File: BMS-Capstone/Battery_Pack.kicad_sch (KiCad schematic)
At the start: 0 parts

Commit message: Added cells
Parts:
- added BT1, BT2, BT3, BT4, BT5, BT6, BT7: Battery_Cell, cell:keystone 254 18650, symbol Device:Battery_Cell
- added J1: Conn_01x12_Socket, symbol Connector:Conn_01x12_Socket
- added J2: Conn_01x02_Socket, symbol Connector:Conn_01x02_Socket
- added K1: J107F1CS203VDC.80, Relay_THT:Relay_SPST-NO_Fujitsu_FTR-LYAA005x_FormA_Vertical, symbol Relay:Fujitsu_FTR-LYAA005x
- added TH1, TH2, TH3: Thermistor, symbol Device:Thermistor
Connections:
- new net: BT1.1 (+), BT2.2 (-), J1.2 (Pin_2)
- new net: BT4.1 (+), BT5.2 (-), J1.5 (Pin_5)
- new net: BT3.1 (+), BT4.2 (-), J1.4 (Pin_4)
- new net: BT6.1 (+), BT7.2 (-), J1.7 (Pin_7)
- new net: BT5.1 (+), BT6.2 (-), J1.6 (Pin_6)
- new net: BT2.1 (+), BT3.2 (-), J1.3 (Pin_3)
- new net: BT7.1 (+), J1.8 (Pin_8), K1.13
- new net: J1.9 (Pin_9), K1.A1
- new net: J2.1 (Pin_1), K1.14
- new net GND: BT1.2 (-), J1.1 (Pin_1), J2.2 (Pin_2), K1.A2, TH1.2, TH2.2, TH3.2
- new net TH1: J1.10 (Pin_10), TH1.1
- new net TH2: J1.11 (Pin_11), TH2.1
- new net TH3: J1.12 (Pin_12), TH3.1

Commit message: Routed Cell Board
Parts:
- removed K1: J107F1CS203VDC.80, Relay_THT:Relay_SPST-NO_Fujitsu_FTR-LYAA005x_FormA_Vertical, symbol Relay:Fujitsu_FTR-LYAA005x
- added K1: J107F1CS203VDC.80, cell:3_3v relay, symbol Relay:DIPxx-1Cxx-51x
- J1: footprint (none) -> Connector_PinHeader_2.54mm:PinHeader_1x12_P2.54mm_Vertical
- J2: footprint (none) -> cell:XT60
- TH1, TH2, TH3: footprint (none) -> Resistor_THT:R_Axial_DIN0204_L3.6mm_D1.6mm_P2.54mm_Vertical
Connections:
- net GND: now also K1.2
- net at BT7.1 (+), J1.8 (Pin_8): now also K1.7, K1.8
- net at J1.9 (Pin_9): now also K1.6
- net at J2.1 (Pin_1): now also K1.14
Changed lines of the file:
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@@
+	)
+	(symbol
+		(lib_id "Relay:DIPxx-1Cxx-51x")
+		(at 129.54 57.15 0)
+		(unit 1)
+		(exclude_from_sim no)
+		(in_bom yes)
+		(on_board yes)
+		(dnp no)
+		(fields_autoplaced yes)
+		(property "Reference" "K1"
+			(at 140.97 55.8799 0)
+			(effects
+				(font
+					(size 1.27 1.27)
+				)
+				(justify left)
+			)
+		)
+		(property "Value" "J107F1CS203VDC.80"
+			(at 140.97 58.4199 0)
+			(effects
+				(font
+					(size 1.27 1.27)
+				)
+				(justify left)
+			)
+		)
+		(property "Footprint" "cell:3_3v relay"
+			(at 140.97 58.42 0)
+			(effects
+				(font
+					(size 1.27 1.27)
+				)
+				(justify left)
+				(hide yes)
+			)
+		)
+		(property "Datasheet" "https://standexelectronics.com/wp-content/uploads/datasheet_reed_relay_DIP.pdf"
+			(at 129.54 57.15 0)
+			(effects
+				(font
+					(size 1.27 1.27)
+				)
+				(hide yes)
+			)
+		)
+		(property "Description" "Standex Meder DIP reed relay, SPDT"
+			(at 129.54 57.15 0)
+			(effects
+				(font
+					(size 1.27 1.27)
+				)
+				(hide yes)
+			)
+		)
+		(pin "1"
+		)
+		(pin "8"
+		)
+		(pin "6"
+		)
+		(pin "14"
+		)
+		(pin "7"
+		)
+		(pin "2"
+		)
+		(instances
+			(project ""
+				(path "/f2da9442-ca05-4687-a880-d5cd24c39f1d/cf34981b-cbae-442d-9f72-9ae4895e9d63"
+					(reference "K1")
+					(unit 1)
+				)
+			)
+		)
 	)
 	(symbol
@@
 			)
 		)
-		(property "Footprint" ""
+		(property "Footprint" "Connector_PinHeader_2.54mm:PinHeader_1x12_P2.54mm_Vertical"
 			(at 50.8 111.76 0)
 			(effects
@@
 	)
 	(symbol
-		(lib_id "Relay:Fujitsu_FTR-LYAA005x")
-		(at 129.54 57.15 0)
-		(unit 1)
-		(exclude_from_sim no)
-		(in_bom yes)
-		(on_board yes)
-		(dnp no)
-		(fields_autoplaced yes)
-		(property "Reference" "K1"
-			(at 140.97 55.8799 0)
-			(effects
-				(font
-					(size 1.27 1.27)
-				)
-				(justify left)
-			)
-		)
-		(property "Value" "J107F1CS203VDC.80"
-			(at 140.97 58.4199 0)
-			(effects
-				(font
-					(size 1.27 1.27)
-				)
-				(justify left)
-			)
-		)
-		(property "Footprint" "Relay_THT:Relay_SPST-NO_Fujitsu_FTR-LYAA005x_FormA_Vertical"
-			(at 140.97 58.42 0)
-			(effects
-				(font
-					(size 1.27 1.27)
-				)
-				(justify left)
-				(hide yes)
-			)
-		)
-		(property "Datasheet" "https://www.fujitsu.com/sg/imagesgig5/ftr-ly.pdf"
-			(at 147.32 60.96 0)
-			(effects
-				(font
-					(size 1.27 1.27)
-				)
-				(justify left)
-				(hide yes)
-			)
-		)
-		(property "Description" "Relay, SPST Form A, vertical mount, 5-60V coil, 6A, 250VAC, 28 x 5 x 15mm"
-			(at 129.54 57.15 0)
-			(effects
-				(font
-					(size 1.27 1.27)
-				)
-				(hide yes)
-			)
-		)
-		(pin "A1"
-		)
-		(pin "A2"
-		)
-		(pin "13"
-		)
-		(pin "14"
-		)
-		(instances
-			(project ""
-				(path "/f2da9442-ca05-4687-a880-d5cd24c39f1d/cf34981b-cbae-442d-9f72-9ae4895e9d63"
-					(reference "K1")
-					(unit 1)
-				)
-			)
-		)
-	)
-	(symbol
 		(lib_id "Device:Battery_Cell")
 		(at 134.62 104.14 0)
@@
 			)
 		)
-		(property "Footprint" ""
+		(property "Footprint" "Resistor_THT:R_Axial_DIN0204_L3.6mm_D1.6mm_P2.54mm_Vertical"
 			(at 157.48 80.01 0)
 			(effects
@@
 			)
 		)
-		(property "Footprint" ""
+		(property "Footprint" "Resistor_THT:R_Axial_DIN0204_L3.6mm_D1.6mm_P2.54mm_Vertical"
 			(at 157.48 114.3 0)
 			(effects
@@
 			)
 		)
-		(property "Footprint" ""
+		(property "Footprint" "Resistor_THT:R_Axial_DIN0204_L3.6mm_D1.6mm_P2.54mm_Vertical"
 			(at 157.48 151.13 0)
 			(effects
@@
 			)
 		)
-		(property "Footprint" ""
+		(property "Footprint" "cell:XT60"
 			(at 137.16 38.1 0)
 			(effects

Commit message: Added fuse
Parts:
- added F1: Fuse, Fuse:Fuseholder_Blade_Mini_Keystone_3568, symbol Device:Fuse
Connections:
- net GND: now also F1.2; no longer BT1.2 (-), J1.1 (Pin_1)
- new net: BT1.2 (-), F1.1, J1.1 (Pin_1)
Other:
- moved on the sheet: J2, K1
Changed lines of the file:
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@@
+	)
+	(junction
+		(at 134.62 72.39)
+		(diameter 0)
+		(color 0 0 0 0)
 	)
 	(junction
@@
 	)
 	(junction
-		(at 134.62 72.39)
-		(diameter 0)
-		(color 0 0 0 0)
-	)
-	(junction
 		(at 134.62 121.92)
 		(diameter 0)
@@
 	(wire
 		(pts
+			(xy 134.62 167.64) (xy 134.62 166.37)
+		)
+		(stroke
+			(width 0)
+			(type default)
+		)
+	)
+	(wire
+		(pts
 			(xy 134.62 121.92) (xy 100.33 121.92)
 		)
@@
 	(wire
 		(pts
+			(xy 134.62 59.69) (xy 134.62 72.39)
+		)
+		(stroke
+			(width 0)
+			(type default)
+		)
+	)
+	(wire
+		(pts
 			(xy 134.62 148.59) (xy 134.62 147.32)
 		)
@@
 	(wire
 		(pts
-			(xy 134.62 64.77) (xy 134.62 72.39)
-		)
-		(stroke
-			(width 0)
-			(type default)
-		)
-	)
-	(wire
-		(pts
 			(xy 88.9 72.39) (xy 134.62 72.39)
 		)
@@
 	(wire
 		(pts
-			(xy 85.09 104.14) (xy 85.09 49.53)
+			(xy 85.09 104.14) (xy 85.09 44.45)
 		)
 		(stroke
@@
 	(wire
 		(pts
-			(xy 85.09 49.53) (xy 124.46 49.53)
+			(xy 85.09 44.45) (xy 124.46 44.45)
+		)
+		(stroke
+			(width 0)
+			(type default)
+		)
+	)
+	(wire
+		(pts
+			(xy 134.62 158.75) (xy 134.62 156.21)
 		)
 		(stroke
@@
 	(wire
 		(pts
-			(xy 137.16 43.18) (xy 137.16 49.53)
+			(xy 137.16 38.1) (xy 137.16 44.45)
 		)
 		(stroke
@@
 	(symbol
 		(lib_id "Relay:DIPxx-1Cxx-51x")
-		(at 129.54 57.15 0)
+		(at 129.54 52.07 0)
 		(unit 1)
 		(exclude_from_sim no)
@@
 		(fields_autoplaced yes)
 		(property "Reference" "K1"
-			(at 140.97 55.8799 0)
+			(at 140.97 50.7999 0)
 			(effects
 				(font
@@
 		)
 		(property "Value" "J107F1CS203VDC.80"
-			(at 140.97 58.4199 0)
+			(at 140.97 53.3399 0)
 			(effects
 				(font
@@
 		)
 		(property "Footprint" "cell:3_3v relay"
-			(at 140.97 58.42 0)
+			(at 140.97 53.34 0)
 			(effects
 				(font
@@
 		)
 		(property "Datasheet" "https://standexelectronics.com/wp-content/uploads/datasheet_reed_relay_DIP.pdf"
-			(at 129.54 57.15 0)
+			(at 129.54 52.07 0)
 			(effects
 				(font
@@
 		)
 		(property "Description" "Standex Meder DIP reed relay, SPDT"
-			(at 129.54 57.15 0)
+			(at 129.54 52.07 0)
 			(effects
 				(font
@@
 	)
 	(symbol
+		(lib_id "Device:Fuse")
+		(at 134.62 162.56 0)
+		(unit 1)
+		(exclude_from_sim no)
+		(in_bom yes)
+		(on_board yes)
+		(dnp no)
+		(fields_autoplaced yes)
+		(property "Reference" "F1"
+			(at 137.16 161.2899 0)
+			(effects
+				(font
+					(size 1.27 1.27)
+				)
+				(justify left)
+			)
+		)
+		(property "Value" "Fuse"
+			(at 137.16 163.8299 0)
+			(effects
+				(font
+					(size 1.27 1.27)
+				)
+				(justify left)
+			)
+		)
+		(property "Footprint" "Fuse:Fuseholder_Blade_Mini_Keystone_3568"
+			(at 132.842 162.56 90)
+			(effects
+				(font
+					(size 1.27 1.27)
+				)
+				(hide yes)
+			)
+		)
+		(property "Datasheet" "~"
+			(at 134.62 162.56 0)
+			(effects
+				(font
+					(size 1.27 1.27)
+				)
+				(hide yes)
+			)
+		)
+		(property "Description" "Fuse"
+			(at 134.62 162.56 0)
+			(effects
+				(font
+					(size 1.27 1.27)
+				)
+				(hide yes)
+			)
+		)
+		(pin "1"
+		)
+		(pin "2"
+		)
+		(instances
+			(project "BMS"
+				(path "/f2da9442-ca05-4687-a880-d5cd24c39f1d/cf34981b-cbae-442d-9f72-9ae4895e9d63"
+					(reference "F1")
+					(unit 1)
+				)
+			)
+		)
+	)
+	(symbol
 		(lib_id "Device:Battery_Cell")
 		(at 134.62 104.14 0)
@@
 	(symbol
 		(lib_id "power:GND")
-		(at 134.62 156.21 0)
+		(at 134.62 167.64 0)
 		(unit 1)
 		(exclude_from_sim no)
@@
 		(fields_autoplaced yes)
 		(property "Reference" "#PWR01"
-			(at 134.62 162.56 0)
+			(at 134.62 173.99 0)
 			(effects
 				(font
@@
 		)
 		(property "Value" "GND"
-			(at 134.62 161.29 0)
+			(at 134.62 172.72 0)
 			(effects
 				(font
@@
 		)
 		(property "Footprint" ""
-			(at 134.62 156.21 0)
+			(at 134.62 167.64 0)
 			(effects
 				(font
@@
 		)
 		(property "Datasheet" ""
-			(at 134.62 156.21 0)
+			(at 134.62 167.64 0)
 			(effects
 				(font
@@
 		)
 		(property "Description" "Power symbol creates a global label with name \"GND\" , ground"
-			(at 134.62 156.21 0)
+			(at 134.62 167.64 0)
 			(effects
 				(font
@@
 	(symbol
 		(lib_id "power:GND")
-		(at 139.7 43.18 0)
+		(at 139.7 38.1 0)
 		(unit 1)
 		(exclude_from_sim no)
@@
 		(fields_autoplaced yes)
 		(property "Reference" "#PWR06"
-			(at 139.7 49.53 0)
+			(at 139.7 44.45 0)
 			(effects
 				(font
@@
 		)
 		(property "Value" "GND"
-			(at 139.7 48.26 0)
+			(at 139.7 43.18 0)
 			(effects
 				(font
@@
 		)
 		(property "Footprint" ""
-			(at 139.7 43.18 0)
+			(at 139.7 38.1 0)
 			(effects
 				(font
@@
 		)
 		(property "Datasheet" ""
-			(at 139.7 43.18 0)
+			(at 139.7 38.1 0)
 			(effects
 				(font
@@
 		)
 		(property "Description" "Power symbol creates a global label with name \"GND\" , ground"
-			(at 139.7 43.18 0)
+			(at 139.7 38.1 0)
 			(effects
 				(font
@@
 	(symbol
 		(lib_id "power:GND")
-		(at 124.46 64.77 0)
+		(at 124.46 59.69 0)
 		(unit 1)
 		(exclude_from_sim no)
@@
 		(fields_autoplaced yes)
 		(property "Reference" "#PWR05"
-			(at 124.46 71.12 0)
+			(at 124.46 66.04 0)
 			(effects
 				(font
@@
 		)
 		(property "Value" "GND"
-			(at 124.46 69.85 0)
+			(at 124.46 64.77 0)
 			(effects
 				(font
@@
 		)
 		(property "Footprint" ""
-			(at 124.46 64.77 0)
+			(at 124.46 59.69 0)
 			(effects
 				(font
@@
 		)
 		(property "Datasheet" ""
-			(at 124.46 64.77 0)
+			(at 124.46 59.69 0)
 			(effects
 				(font
@@
 		)
 		(property "Description" "Power symbol creates a global label with name \"GND\" , ground"
-			(at 124.46 64.77 0)
+			(at 124.46 59.69 0)
 			(effects
 				(font
@@
 	(symbol
 		(lib_id "Connector:Conn_01x02_Socket")
-		(at 137.16 38.1 90)
+		(at 137.16 33.02 90)
 		(unit 1)
 		(exclude_from_sim no)
@@
 		(fields_autoplaced yes)
 		(property "Reference" "J2"
-			(at 140.97 37.4649 90)
+			(at 140.97 32.3849 90)
 			(effects
 				(font
@@
 		)
 		(property "Value" "Conn_01x02_Socket"
-			(at 140.97 40.0049 90)
+			(at 140.97 34.9249 90)
 			(effects
 				(font
@@
 		)
 		(property "Footprint" "cell:XT60"
-			(at 137.16 38.1 0)
+			(at 137.16 33.02 0)
 			(effects
 				(font
@@
 		)
 		(property "Datasheet" "~"
-			(at 137.16 38.1 0)
+			(at 137.16 33.02 0)
 			(effects
 				(font
@@
 		)
 		(property "Description" "Generic connector, single row, 01x02, script generated"
-			(at 137.16 38.1 0)
-			(effects
-				(font
+			(at 137.16 33.02 0)
+			(effects
+				(font

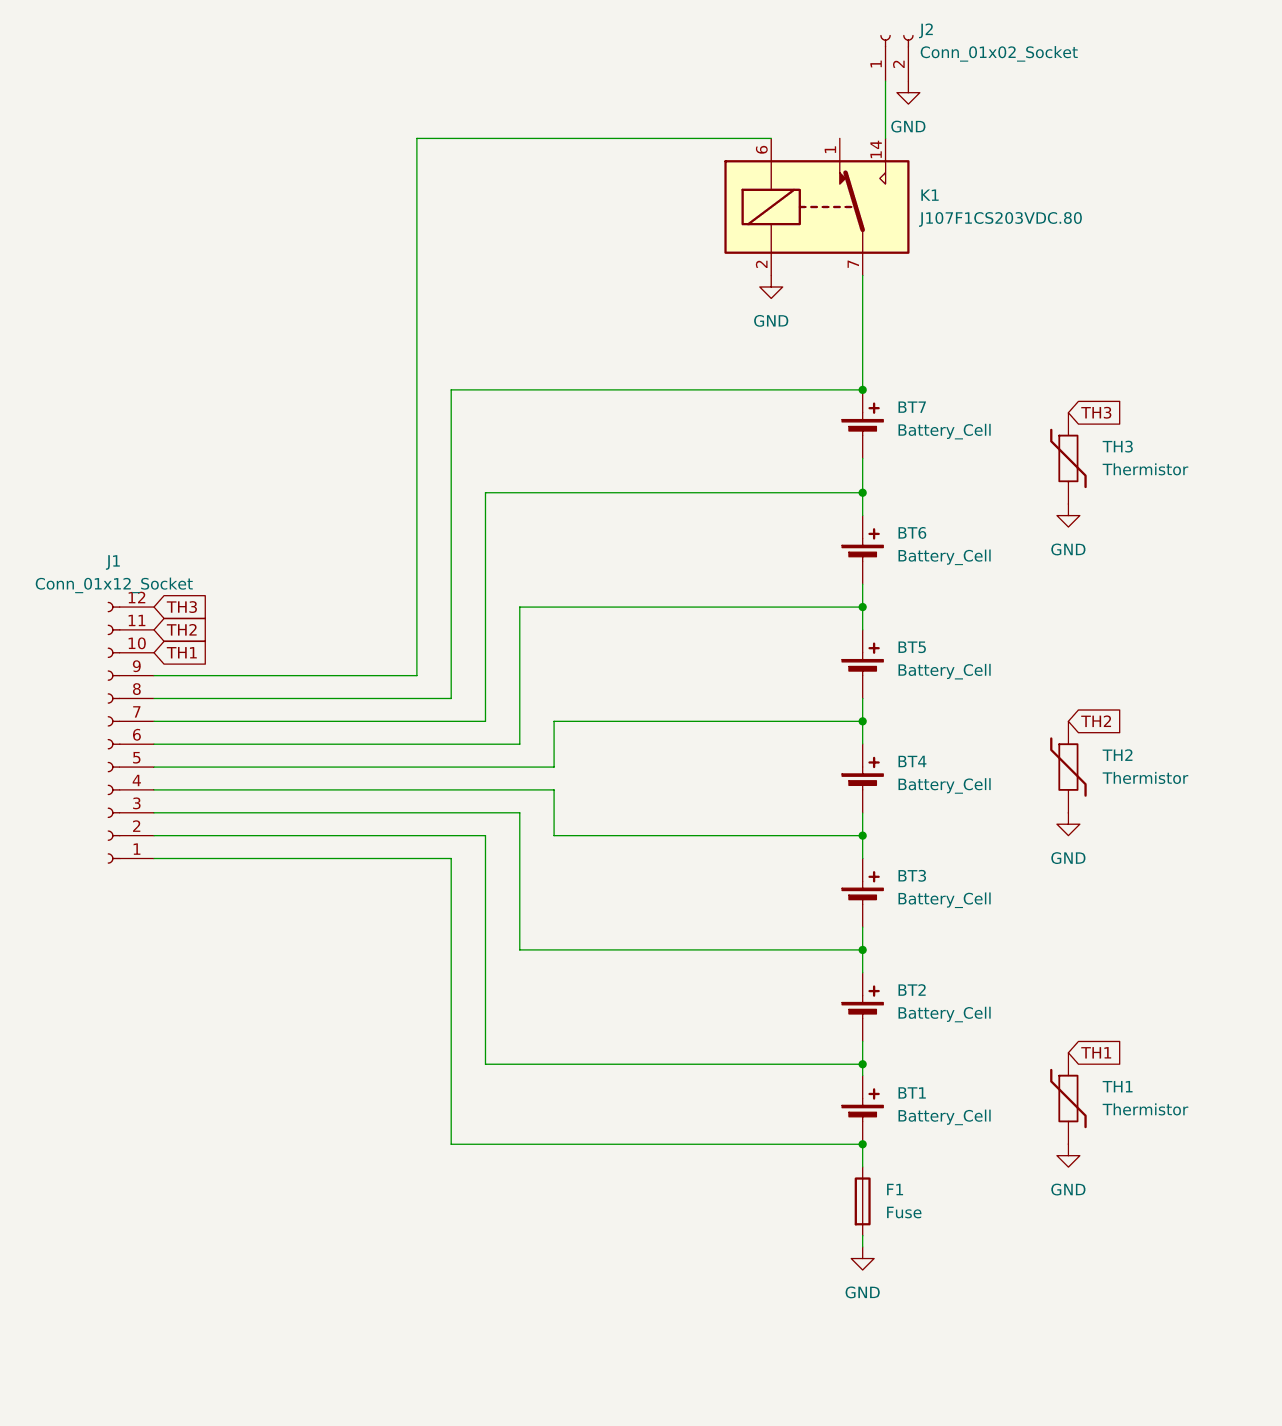
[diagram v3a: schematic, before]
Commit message: Current Sense Resistor
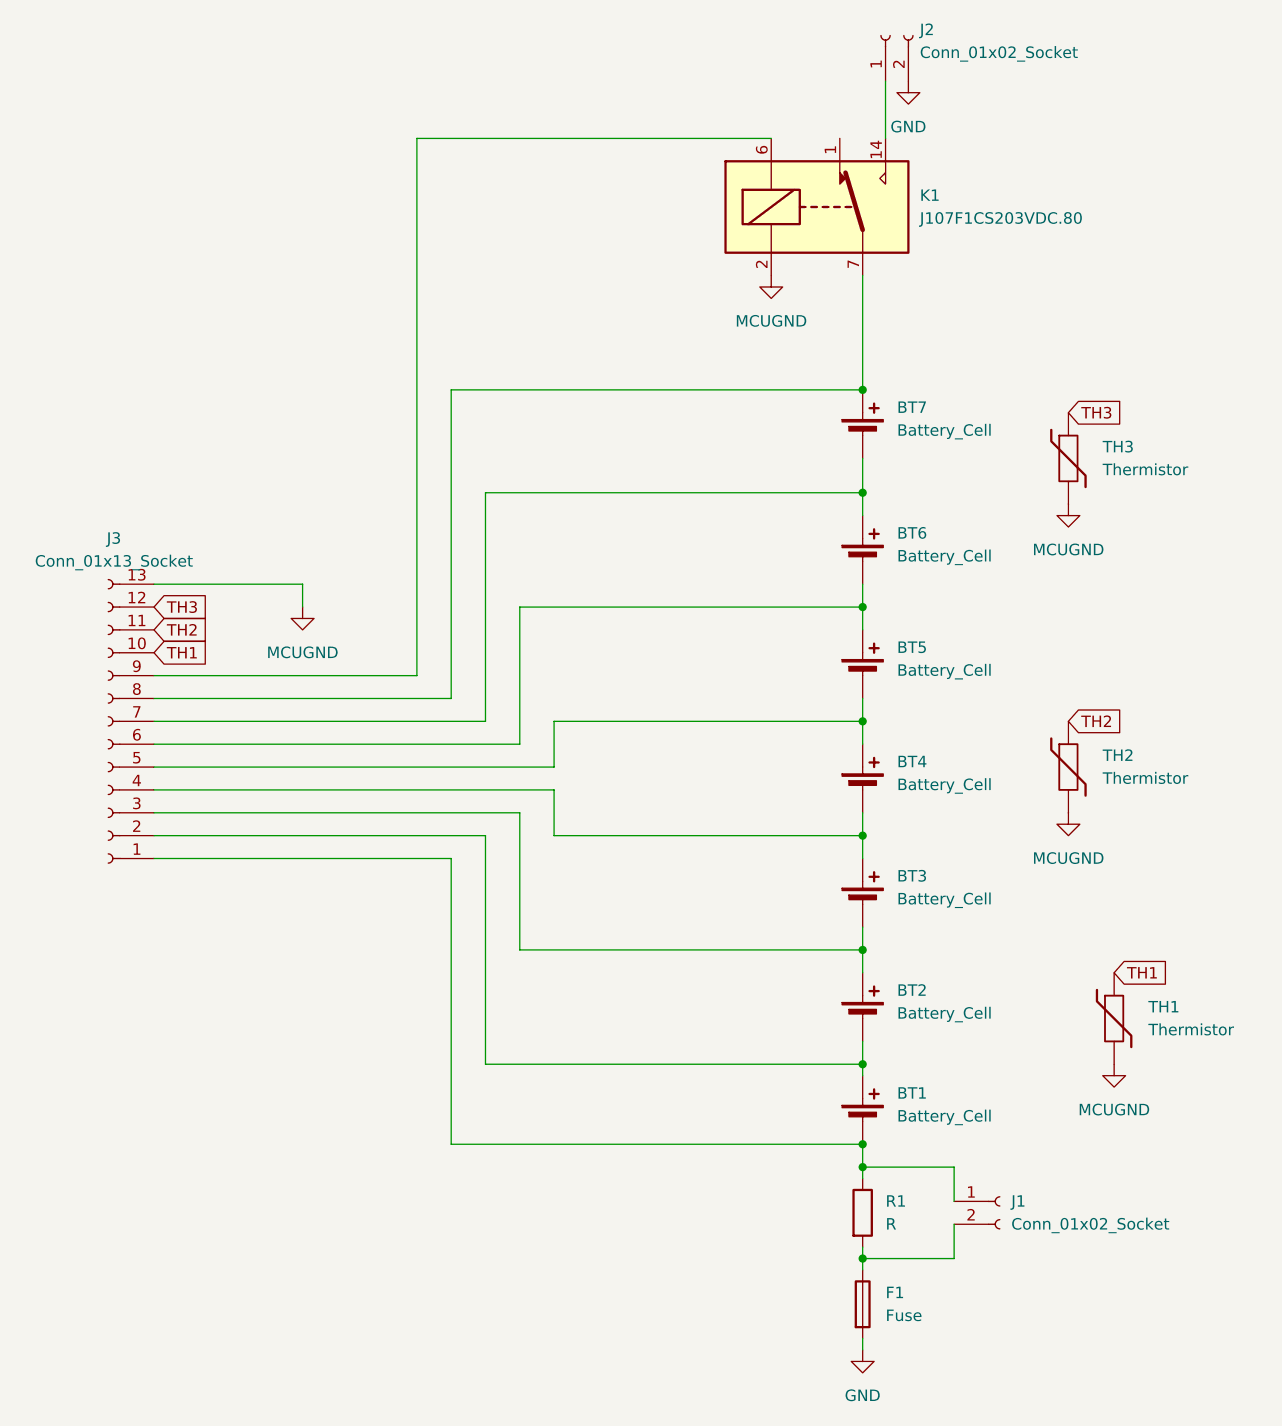
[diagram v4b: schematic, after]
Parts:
- removed J1: Conn_01x12_Socket, Connector_PinHeader_2.54mm:PinHeader_1x12_P2.54mm_Vertical, symbol Connector:Conn_01x12_Socket
- added J1: Conn_01x02_Socket, Connector_PinHeader_2.54mm:PinHeader_1x02_P2.54mm_Vertical, symbol Connector:Conn_01x02_Socket
- added J3: Conn_01x13_Socket, Connector_PinHeader_2.54mm:PinHeader_1x13_P2.54mm_Vertical, symbol Connector:Conn_01x13_Socket
- added R1: R, Resistor_SMD:R_1210_3225Metric, symbol Device:R
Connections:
- net GND: no longer K1.2, TH1.2, TH2.2, TH3.2
- net TH1: now also J3.10 (Pin_10)
- net TH2: now also J3.11 (Pin_11)
- net TH3: now also J3.12 (Pin_12)
- net at BT1.1 (+), BT2.2 (-): now also J3.2 (Pin_2)
- net at BT1.2 (-): now also J1.1 (Pin_1), J3.1 (Pin_1), R1.1; no longer F1.1
- net at BT4.1 (+), BT5.2 (-): now also J3.5 (Pin_5)
- net at BT3.1 (+), BT4.2 (-): now also J3.4 (Pin_4)
- net at BT6.1 (+), BT7.2 (-): now also J3.7 (Pin_7)
- net at BT5.1 (+), BT6.2 (-): now also J3.6 (Pin_6)
- net at K1.6: now also J3.9 (Pin_9)
- net at BT7.1 (+), K1.7, K1.8: now also J3.8 (Pin_8)
- net at BT2.1 (+), BT3.2 (-): now also J3.3 (Pin_3)
- new net: F1.1, J1.2 (Pin_2), R1.2
- new net MCUGND: J3.13 (Pin_13), K1.2, TH1.2, TH2.2, TH3.2
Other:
- moved on the sheet: F1, TH1
